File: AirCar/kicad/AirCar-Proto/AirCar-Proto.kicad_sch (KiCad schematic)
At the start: 16 parts, among them J1 Conn_01x05, J3 Conn_01x06, J4 PJ-102A, SW2 SW_SPDT, U1 Pico, U2 LM7805_TO220

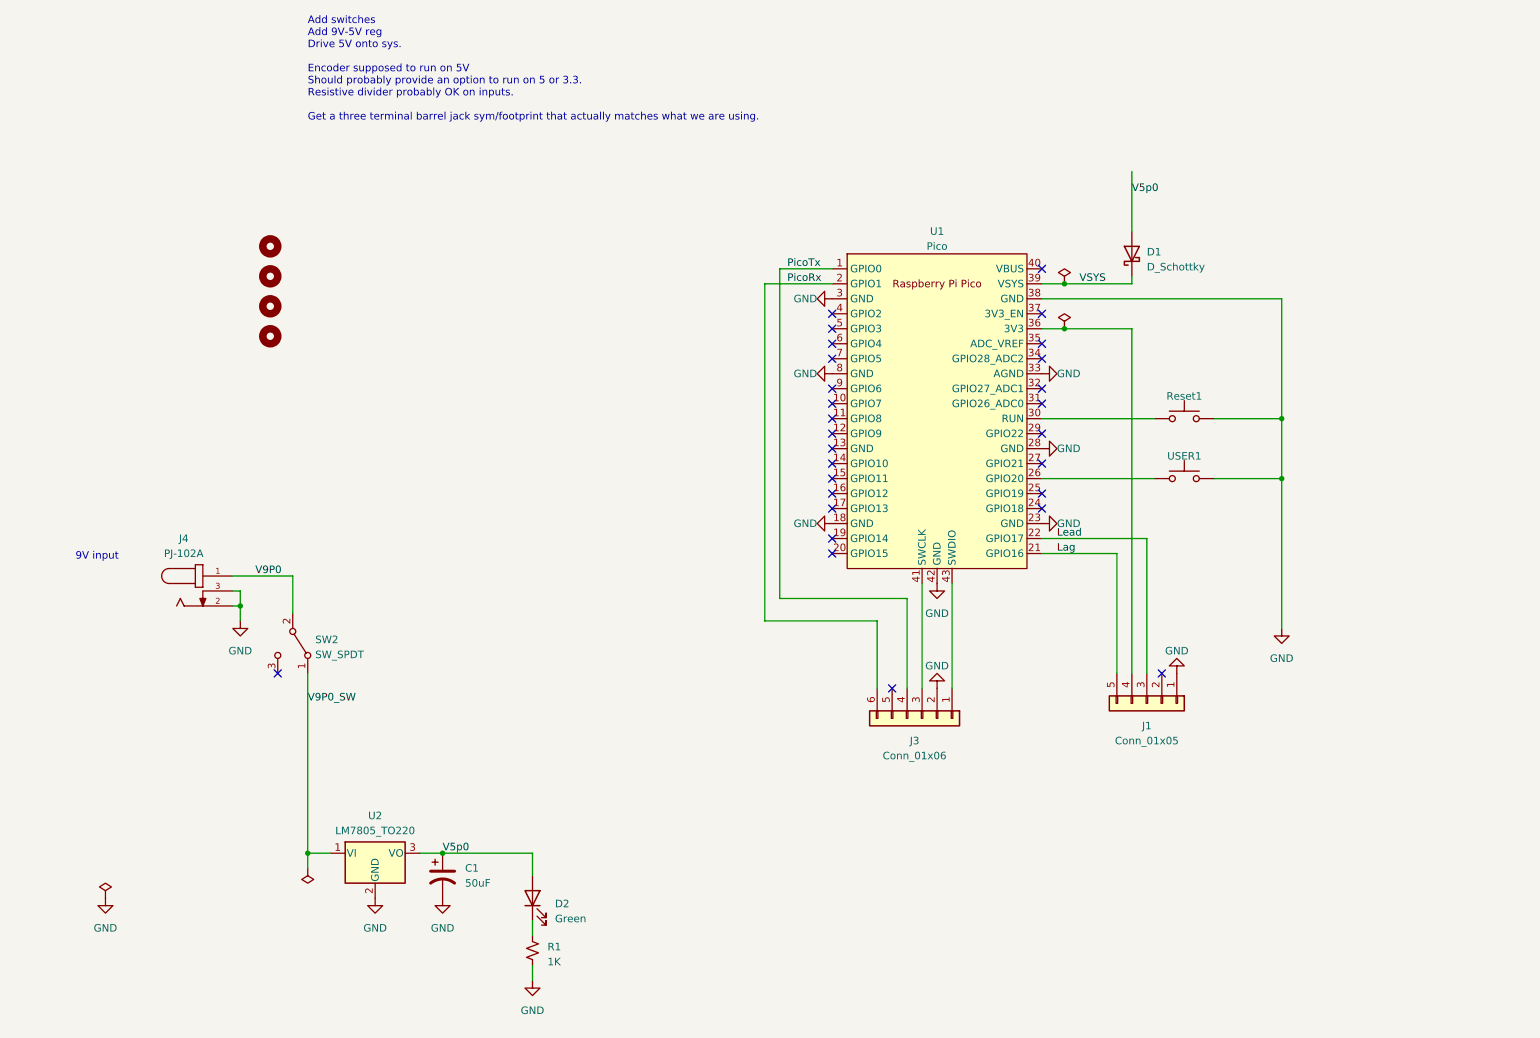
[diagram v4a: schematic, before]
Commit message: work on adding level shifter
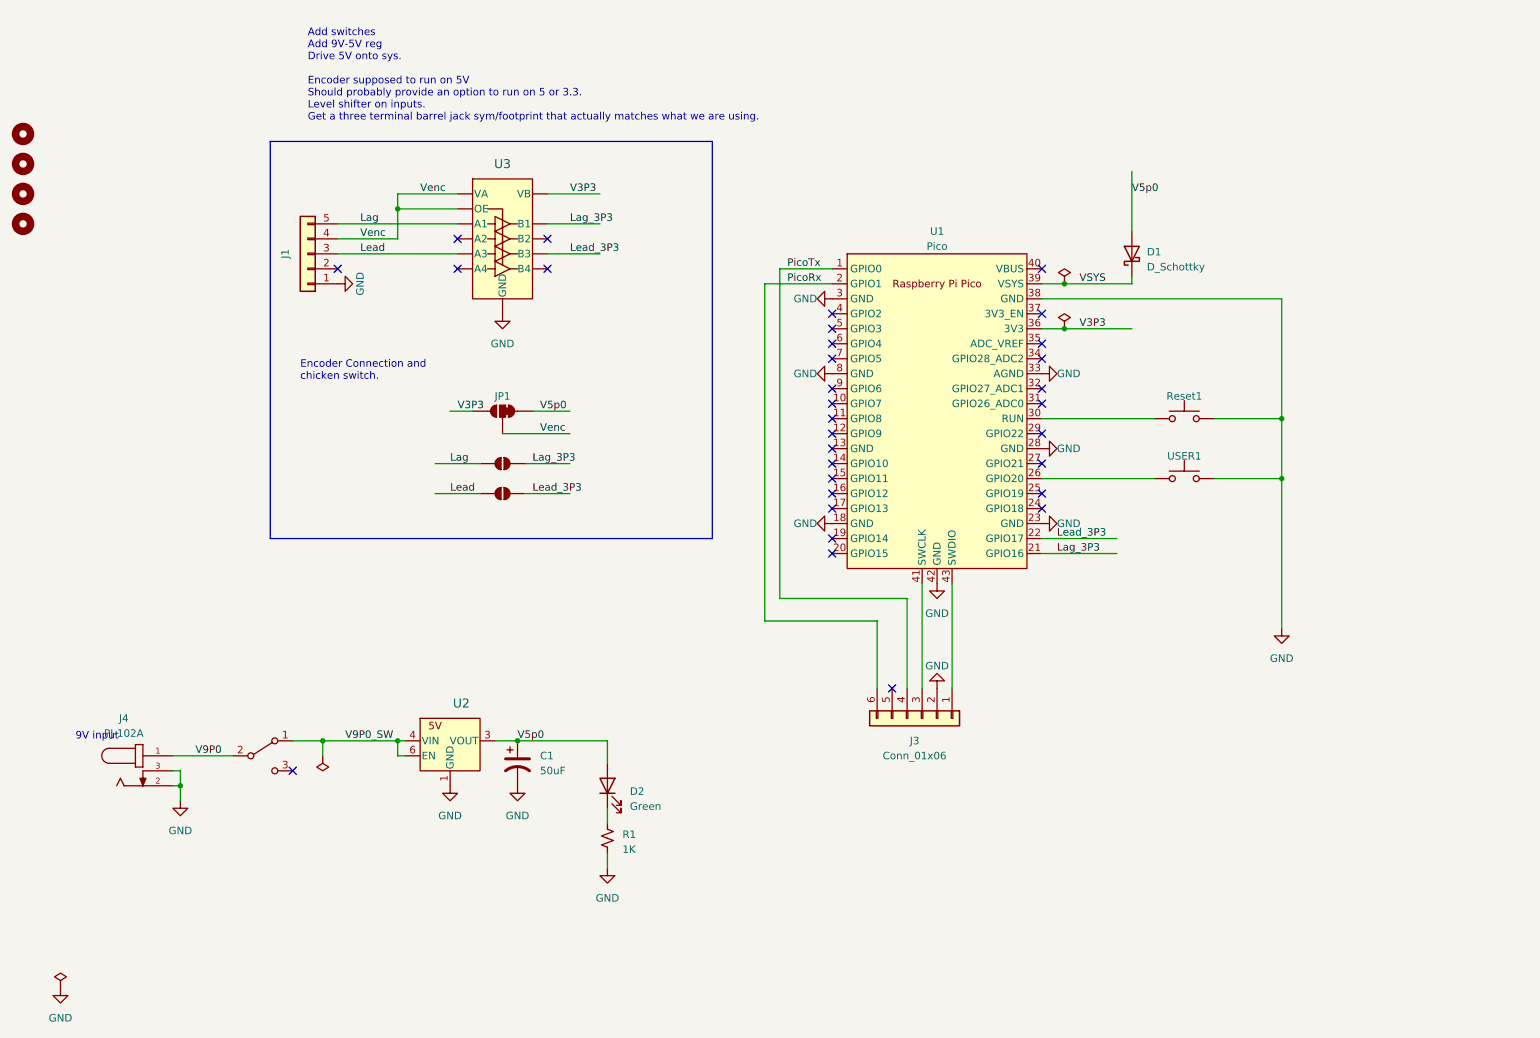
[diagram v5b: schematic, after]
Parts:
- removed U2: LM7805_TO220, Package_TO_SOT_THT:TO-220-3_Vertical, symbol Regulator_Linear:LM7805_TO220
- added JP1: SolderJumper_3_Bridged12, Jumper:SolderJumper-3_P1.3mm_Bridged12_RoundedPad1.0x1.5mm, symbol Jumper:SolderJumper_3_Bridged12
- added JP2, JP3: SolderJumper_2_Open, Jumper:SolderJumper-2_P1.3mm_Open_RoundedPad1.0x1.5mm, symbol Jumper:SolderJumper_2_Open
- added U2: LDL212PU50R, Package_DFN_QFN:DFN-6-1EP_3x3mm_P0.95mm_EP1.7x2.6mm, symbol Local:LDL212PU50R
- added U3: TXU0104BQAR, Library:U_TXU0104_TEX, symbol Local:TXU0104BQAR
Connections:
- net GND: now also U2.1 (GND), U2.7 (GND), U3.15 (GND), U3.7 (GND)
- net Lag: now also JP2.1 (A), U3.2 (A1); no longer U1.21 (GPIO16)
- net Lead: now also JP3.1 (A), U3.4 (A3); no longer U1.22 (GPIO17)
- net V5p0: now also JP1.1 (A), U2.2 (ADJ/sense), U2.3 (VOUT)
- net V9P0_SW: now also U2.4 (VIN), U2.6 (EN)
- net V3P3: now reaches U1.36 (3V3)
- net V3P3: now also JP1.3 (B), U3.14 (VB); no longer J1.4 (Pin_4)
- new net Lag_3P3: JP2.2 (B), U1.21 (GPIO16), U3.13 (B1)
- new net Lead_3P3: JP3.2 (B), U1.22 (GPIO17), U3.11 (B3)
- new net Venc: J1.4 (Pin_4), JP1.2 (C), U3.1 (VA), U3.8 (OE)
- no-connect marks 28 -> 32
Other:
- note added: "Add switches Add 9V-5V reg Drive 5V onto sys. Encoder supposed to run on 5V Should probably provide an option to run on 5 or 3.3. Level shifter on inputs. Get a three terminal barrel jack sym/footprint that actually matches what we are using."
- note added: "Encoder Connection and chicken switch."
- note removed: "Add switches Add 9V-5V reg Drive 5V onto sys. Encoder supposed to run on 5V Should probably provide an option to run on 5 or 3.3. Resistive divider probably OK on inputs. Get a three terminal barrel jack sym/footprint that actually matches what we are using."
- moved on the sheet: C1, D2, J1, J4, R1

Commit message: wip
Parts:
- added J2, J5: Conn_01x20_Socket, Connector_PinHeader_2.54mm:PinHeader_1x20_P2.54mm_Vertical, symbol Connector:Conn_01x20_Socket
- J3: now not fitted
- U1: Digikey (none) -> 2648-SC0915TR-ND
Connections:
- net GND: now also U1.13 (GND), J2.13 (Pin_13), J2.18 (Pin_18), J2.3 (Pin_3), J2.8 (Pin_8), J5.13 (Pin_13), J5.18 (Pin_18), J5.3 (Pin_3), J5.8 (Pin_8)
- net Lag_3P3: now also J2.20 (Pin_20)
- net Lead_3P3: now also J2.19 (Pin_19)
- net PicoRx: now also J5.19 (Pin_19)
- net PicoTx: now also J5.20 (Pin_20)
- net V3P3: now also J2.5 (Pin_5)
- net VSYS: now also J2.2 (Pin_2)
- net at U1.10 (GPIO7): now also J5.11 (Pin_11)
- net at U1.11 (GPIO8): now also J5.10 (Pin_10)
- net at U1.12 (GPIO9): now also J5.9 (Pin_9)
- net at U1.14 (GPIO10): now also J5.7 (Pin_7)
- net at U1.15 (GPIO11): now also J5.6 (Pin_6)
- net at U1.16 (GPIO12): now also J5.5 (Pin_5)
- net at U1.17 (GPIO13): now also J5.4 (Pin_4)
- net at U1.19 (GPIO14): now also J5.2 (Pin_2)
- net at U1.20 (GPIO15): now also J5.1 (Pin_1)
- net at U1.24 (GPIO18): now also J2.17 (Pin_17)
- net at U1.25 (GPIO19): now also J2.16 (Pin_16)
- net at U1.26 (GPIO20), USER1.1, USER1.2: now also J2.15 (Pin_15)
- net at U1.27 (GPIO21): now also J2.14 (Pin_14)
- net at U1.29 (GPIO22): now also J2.12 (Pin_12)
- net at Reset1.1, Reset1.2, U1.30 (RUN): now also J2.11 (Pin_11)
- net at U1.31 (GPIO26_ADC0): now also J2.10 (Pin_10)
- net at U1.32 (GPIO27_ADC1): now also J2.9 (Pin_9)
- net at U1.34 (GPIO28_ADC2): now also J2.7 (Pin_7)
- net at U1.35 (ADC_VREF): now also J2.6 (Pin_6)
- net at U1.37 (3V3_EN): now also J2.4 (Pin_4)
- net at U1.4 (GPIO2): now also J5.17 (Pin_17)
- net at U1.40 (VBUS): now also J2.1 (Pin_1)
- net at U1.5 (GPIO3): now also J5.16 (Pin_16)
- net at U1.6 (GPIO4): now also J5.15 (Pin_15)
- net at U1.7 (GPIO5): now also J5.14 (Pin_14)
- net at U1.9 (GPIO6): now also J5.12 (Pin_12)
- no-connect marks 32 -> 7
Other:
- moved on the sheet: D1, Reset1, U1, USER1

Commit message: switch to some none through hole parts because SMD is easier...
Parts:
- D1: footprint Diode_THT:D_DO-41_SOD81_P7.62mm_Horizontal -> Diode_SMD:D_SOD-123F; Digikey 1N5817-E3/54GITR-ND -> CRS01QCT-ND
- R1: footprint Resistor_THT:R_Axial_DIN0207_L6.3mm_D2.5mm_P10.16mm_Horizontal -> Resistor_SMD:R_0603_1608Metric
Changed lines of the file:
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@@
       (effects (font (size 1.27 1.27)) (justify left))
     )
-    (property "Footprint" "Resistor_THT:R_Axial_DIN0207_L6.3mm_D2.5mm_P10.16mm_Horizontal" (at 121.92 154.94 0)
+    (property "Footprint" "Resistor_SMD:R_0603_1608Metric" (at 121.92 154.94 0)
       (effects (font (size 1.27 1.27)) hide)
     )
@@
       (effects (font (size 1.27 1.27)) (justify right))
     )
-    (property "Footprint" "Diode_THT:D_DO-41_SOD81_P7.62mm_Horizontal" (at 261.62 52.07 0)
+    (property "Footprint" "Diode_SMD:D_SOD-123F" (at 261.62 52.07 0)
       (effects (font (size 1.27 1.27)) hide)
     )
@@
       (effects (font (size 1.27 1.27)) hide)
     )
-    (property "Digikey" "1N5817-E3/54GITR-ND" (at 261.62 52.07 90)
-      (effects (font (size 1.27 1.27)) hide)
-    )
+    (property "Digikey" "CRS01QCT-ND" (at 261.62 52.07 90)
+      (effects (font (size 1.27 1.27)) hide)
+    )

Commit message: possible rev 0.1 candidate
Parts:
- removed J2, J5: Conn_01x20_Socket, Connector_PinHeader_2.54mm:PinHeader_1x20_P2.54mm_Vertical, symbol Connector:Conn_01x20_Socket
- added C2: 0.1uF, Capacitor_SMD:C_0603_1608Metric, symbol Device:C_Small
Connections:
- net GND: now also C2.2
- net Venc: now also C2.1
- no-connect marks 7 -> 31
